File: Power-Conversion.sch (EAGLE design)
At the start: 55 parts, among them J3 AVR_SPI_PROG_3X2NS, Q1 SUM90P10-19L, U1 LM1085IS-3.3, U2 ATMEGA328P_TQFP, U7 LM2678

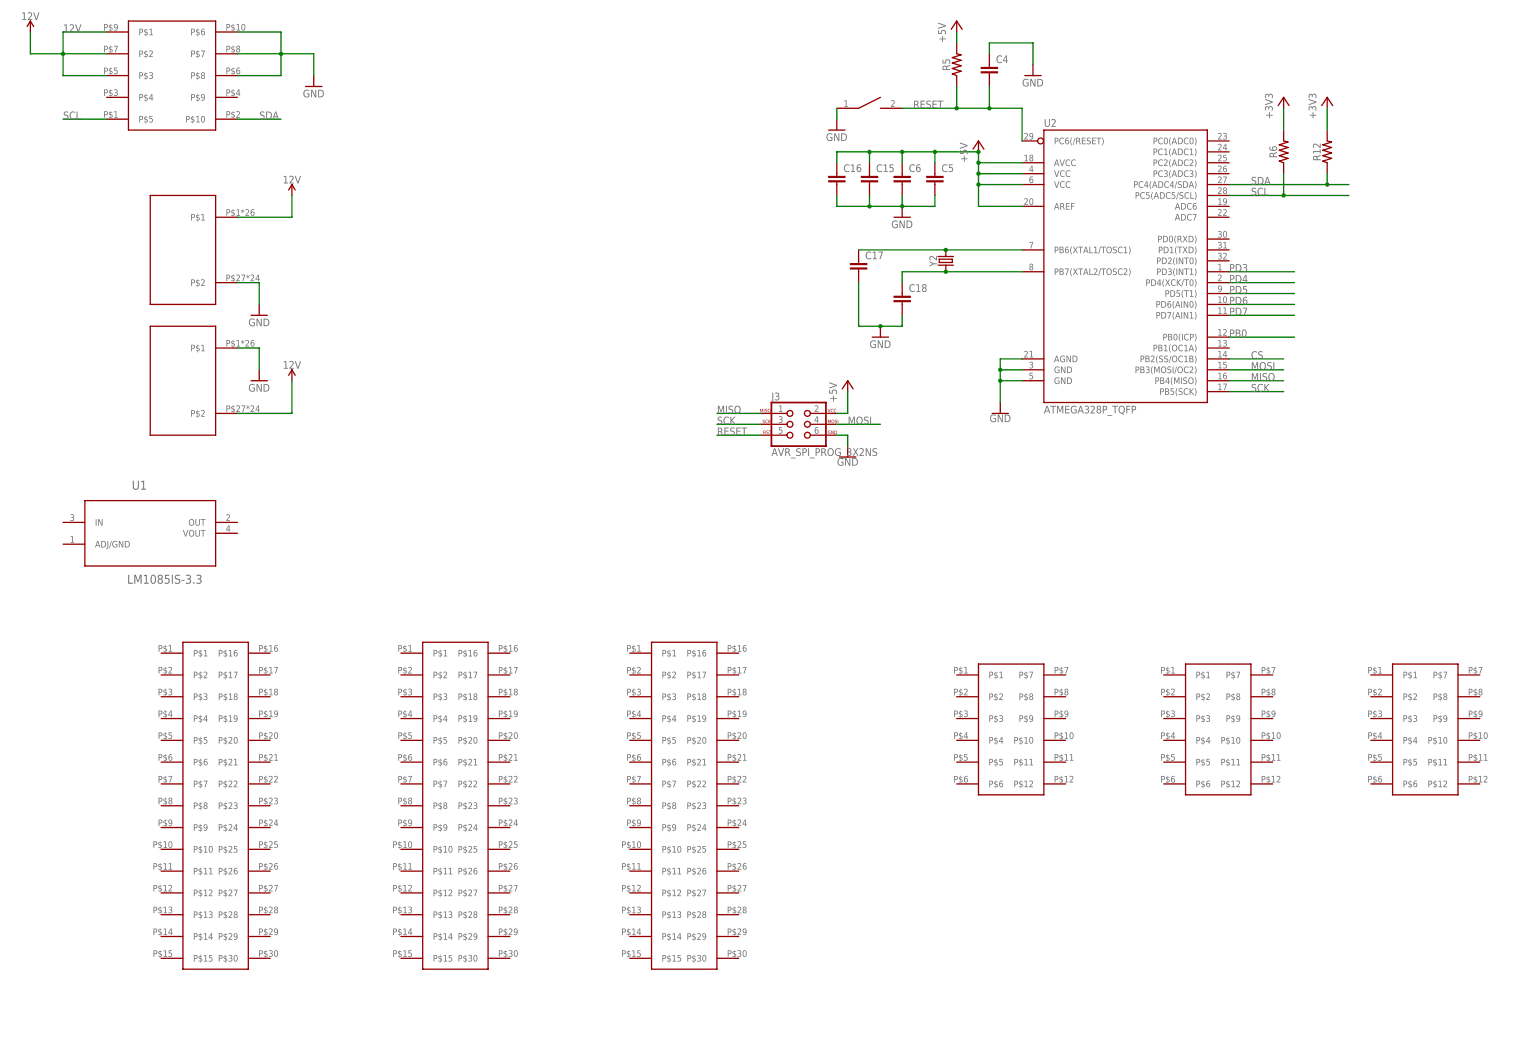
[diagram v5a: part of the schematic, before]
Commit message: Removed micro
removed micro controller and added capacitors to linear regelator
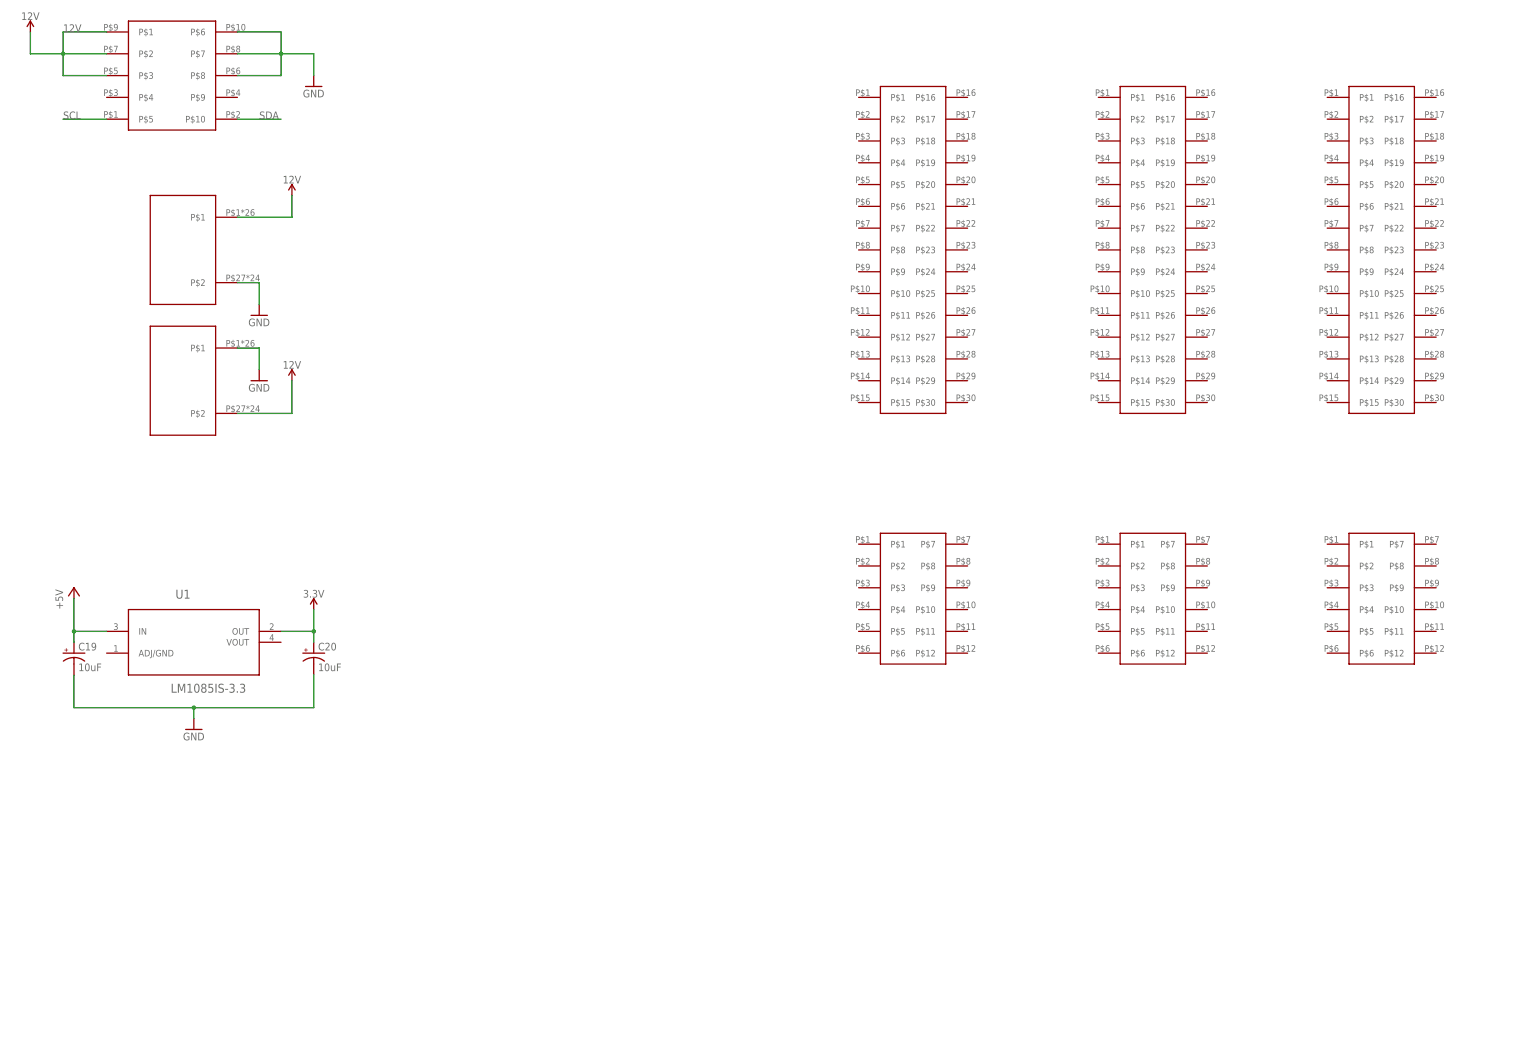
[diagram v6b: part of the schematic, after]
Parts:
- removed C15, C16, C17, C18, C4, C5, C6: (no value), rcl:C-EUC0603
- removed J3: AVR_SPI_PROG_3X2NS, SparkFun-Connectors:AVR_SPI_PROG_3X2NS
- removed R12, R5, R6: (no value), SparkFun-Resistors:RESISTOR0603
- removed RESET: SWITCH, DiscreteComponents:SWITCH
- removed U2: ATMEGA328P_TQFP, SparkFun-IC-Microcontroller:ATMEGA328P_TQFP
- removed Y2: (no value), SparkFun-Clocks:CRYSTALPTH-HC49US
- added C19, C20: 10uF, PowerComponents:C-TANTALUM(10UF_150UF)
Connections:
- removed net +3V3: R12.2, R6.2
- removed net CS: U2.PB2(SS/OC1B)
- removed net MISO: J3.1, U2.PB4(MISO)
- removed net MOSI: J3.4, U2.PB3(MOSI/OC2)
- removed net N$14: C17.1, U2.PB6(XTAL1/TOSC1), Y2.2
- removed net N$15: C18.1, U2.PB7(XTAL2/TOSC2), Y2.1
- removed net PB0: U2.PB0(ICP)
- removed net PD3: U2.PD3(INT1)
- removed net PD4: U2.PD4(XCK/T0)
- removed net PD5: U2.PD5(T1)
- removed net PD6: U2.PD6(AIN0)
- removed net PD7: U2.PD7(AIN1)
- removed net RESET: C4.2, J3.5, R5.1, RESET.P$2, U2.PC6(/RESET)
- removed net SCK: J3.3, U2.PB5(SCK)
- new net 3.3V: C20.+, U1.OUT
- net +5V: now also C19.+, U1.IN; no longer C15.1, C16.1, C5.1, C6.1, J3.2, R5.2, U2.AREF, U2.AVCC, U2.VCC@4, U2.VCC@6
- net GND: now also C19.-, C20.-; no longer C15.2, C16.2, C17.2, C18.2, C4.1, C5.2, C6.2, J3.6, RESET.P$1, U2.AGND, U2.GND@3, U2.GND@5
- net SCL: no longer R6.1, U2.PC5(ADC5/SCL)
- net SDA: no longer R12.1, U2.PC4(ADC4/SDA)
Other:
- moved on the sheet: U1

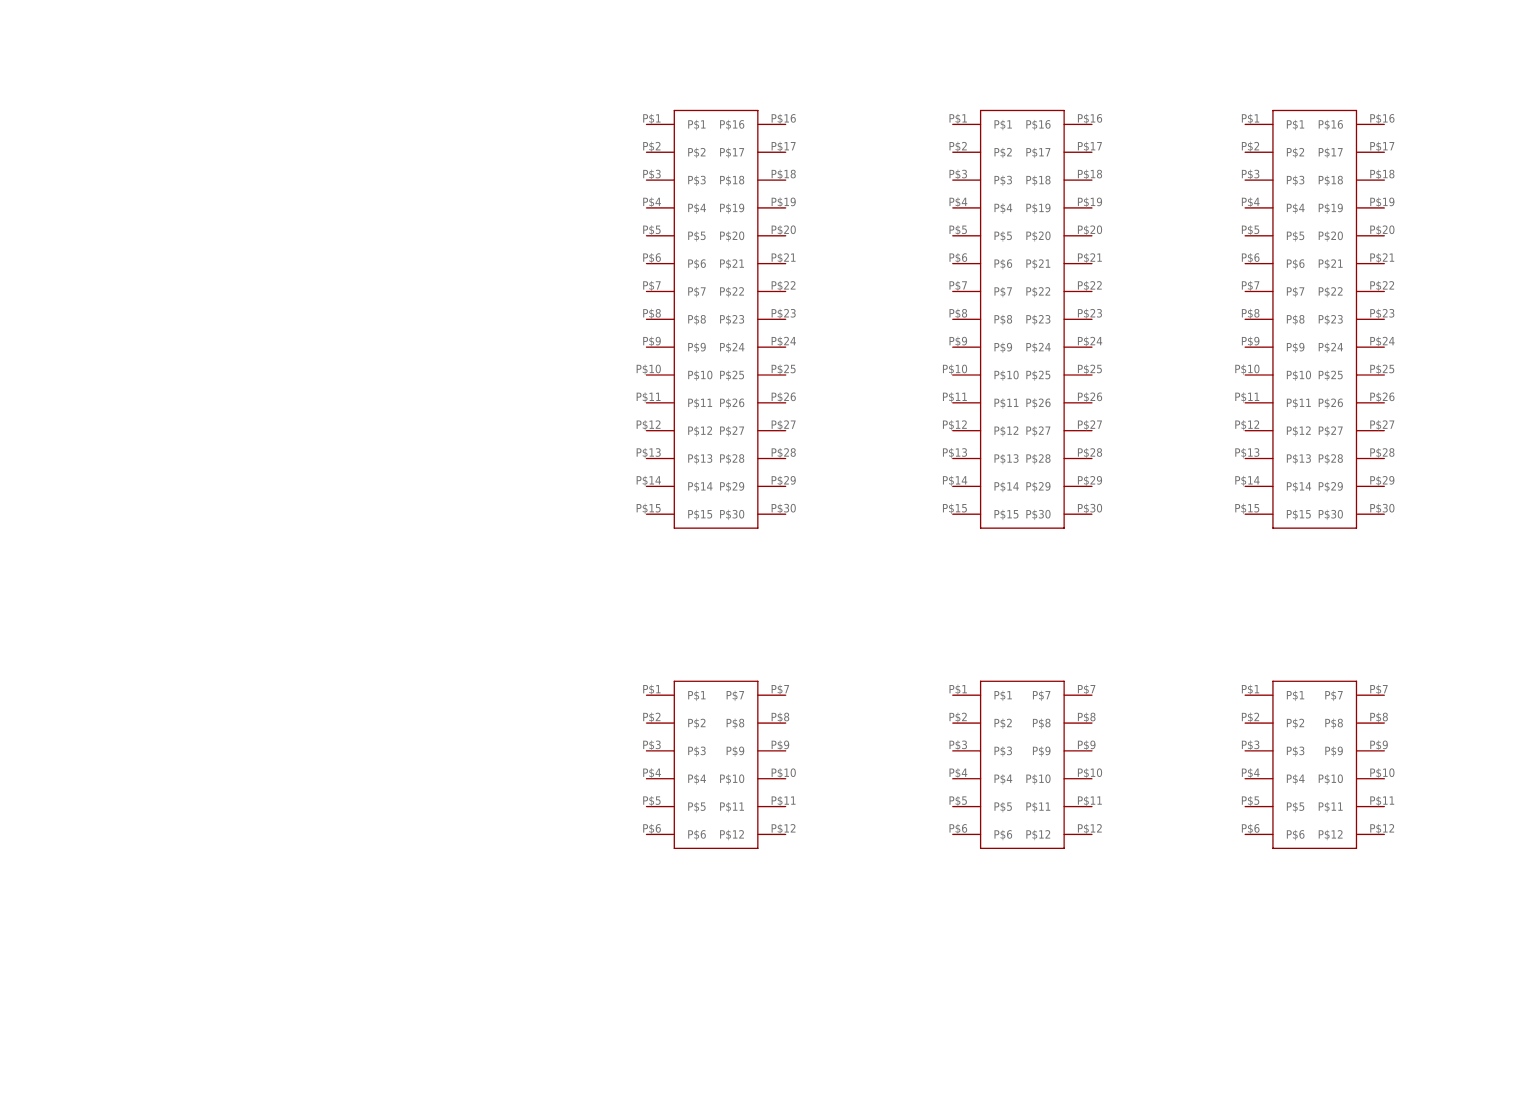
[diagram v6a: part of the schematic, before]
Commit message: Connected the connectors
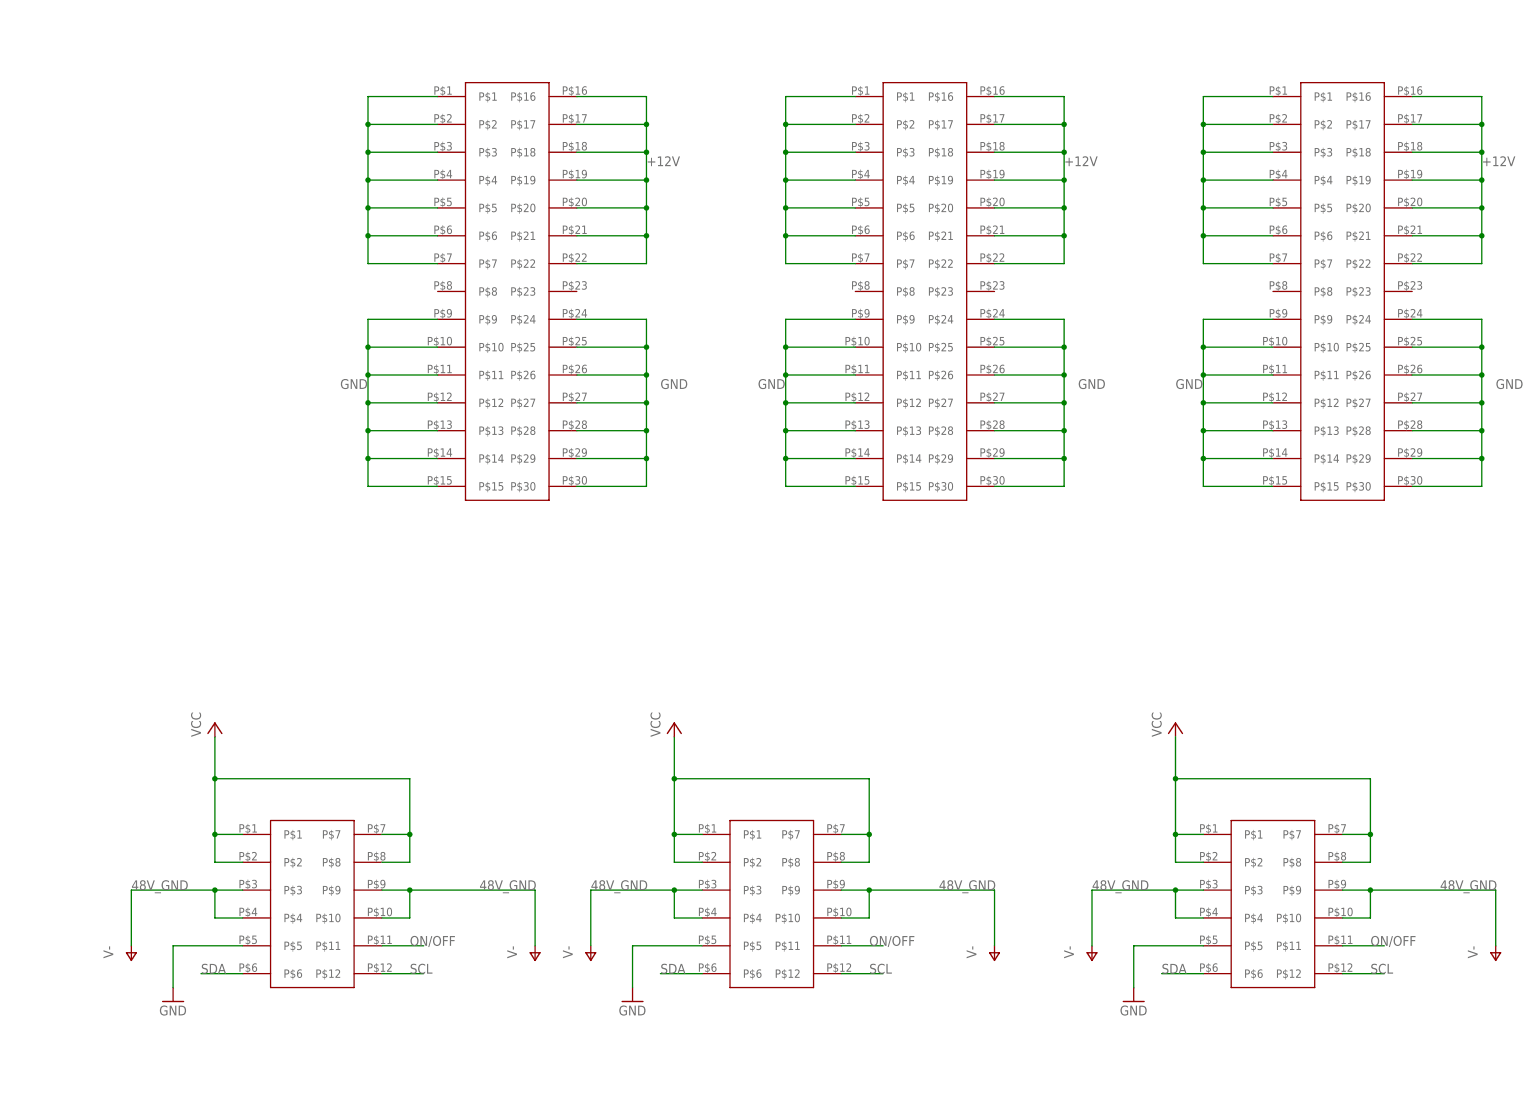
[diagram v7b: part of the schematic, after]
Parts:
- removed U$16: POWER_BRICK_CONNECTORS(2X6), MotherBoardParts2:POWER_BRICK_CONNECTORS(2X6)
- added U$17: POWER_BRICK_CONNECTORS(2X15), MotherBoardParts2:POWER_BRICK_CONNECTORS(2X15)
- U$13: value POWER_BRICK_CONNECTORS(2X15) -> POWER_BRICK_CONNECTORS(2X6); device MotherBoardParts2:POWER_BRICK_CONNECTORS(2X15) -> MotherBoardParts2:POWER_BRICK_CONNECTORS(2X6)
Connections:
- new net ON/OFF: U$13.P$11, U$14.P$11, U$15.P$11
- new net VCC: U$13.P$1, U$13.P$2, U$13.P$7, U$13.P$8, U$14.P$1, U$14.P$2, U$14.P$7, U$14.P$8, U$15.P$1, U$15.P$2, U$15.P$7, U$15.P$8
- net +12V: now also U$11.P$1, U$11.P$16, U$11.P$17, U$11.P$18, U$11.P$19, U$11.P$2, U$11.P$20, U$11.P$21, U$11.P$22, U$11.P$3, U$11.P$4, U$11.P$5, U$11.P$6, U$11.P$7, U$12.P$1, U$12.P$16, U$12.P$17, U$12.P$18, U$12.P$19, U$12.P$2, U$12.P$20, U$12.P$21, U$12.P$22, U$12.P$3, U$12.P$4, U$12.P$5, U$12.P$6, U$12.P$7, U$17.P$1, U$17.P$16, U$17.P$17, U$17.P$18, U$17.P$19, U$17.P$2, U$17.P$20, U$17.P$21, U$17.P$22, U$17.P$3, U$17.P$4, U$17.P$5, U$17.P$6, U$17.P$7
- net 48V_GND: now also U$13.P$10, U$13.P$3, U$13.P$4, U$13.P$9, U$14.P$10, U$14.P$3, U$14.P$4, U$14.P$9, U$15.P$10, U$15.P$3, U$15.P$4, U$15.P$9
- net GND: now also U$11.P$10, U$11.P$11, U$11.P$12, U$11.P$13, U$11.P$14, U$11.P$15, U$11.P$24, U$11.P$25, U$11.P$26, U$11.P$27, U$11.P$28, U$11.P$29, U$11.P$30, U$11.P$9, U$12.P$10, U$12.P$11, U$12.P$12, U$12.P$13, U$12.P$14, U$12.P$15, U$12.P$24, U$12.P$25, U$12.P$26, U$12.P$27, U$12.P$28, U$12.P$29, U$12.P$30, U$12.P$9, U$13.P$5, U$14.P$5, U$15.P$5, U$17.P$10, U$17.P$11, U$17.P$12, U$17.P$13, U$17.P$14, U$17.P$15, U$17.P$24, U$17.P$25, U$17.P$26, U$17.P$27, U$17.P$28, U$17.P$29, U$17.P$30, U$17.P$9
- net SCL: now also U$13.P$12, U$14.P$12, U$15.P$12
- net SDA: now also U$13.P$6, U$14.P$6, U$15.P$6

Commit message: Started Board layout
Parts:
- removed C19, C20: 10uF, PowerComponents:C-TANTALUM(10UF_150UF)
- removed U1: LM1085IS-3.3, PowerComponents:LM1085IS-3.3
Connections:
- removed net 3.3V: C20.+, U1.OUT
- net +5V: no longer C19.+, U1.IN
- net GND: no longer C19.-, C20.-
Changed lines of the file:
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@@
 <part name="GND5" library="supply1" deviceset="GND" device=""/>
 <part name="SUPPLY3" library="SparkFun-PowerSymbols" deviceset="12V" device=""/>
-<part name="U1" library="PowerComponents" deviceset="LM1085IS-3.3" device=""/>
-<part name="C19" library="PowerComponents" deviceset="C-TANTALUM(10UF_150UF)" device="" value="10uF"/>
-<part name="C20" library="PowerComponents" deviceset="C-TANTALUM(10UF_150UF)" device="" value="10uF"/>
-<part name="GND6" library="supply1" deviceset="GND" device=""/>
-<part name="P+6" library="supply1" library_urn="urn:adsk.eagle:library:371" deviceset="+5V" device=""/>
-<part name="SUPPLY4" library="SparkFun-PowerSymbols" deviceset="3.3V" device=""/>
 <part name="U$17" library="MotherBoardParts2" deviceset="POWER_BRICK_CONNECTORS(2X15)" device=""/>
 <part name="U$11" library="MotherBoardParts2" deviceset="POWER_BRICK_CONNECTORS(2X15)" device=""/>
@@
 <instance part="GND5" gate="1" x="83.82" y="502.92"/>
 <instance part="SUPPLY3" gate="G$1" x="17.78" y="515.62"/>
-<instance part="U1" gate="A" x="55.88" y="375.92"/>
-<instance part="C19" gate="G$1" x="27.94" y="370.84"/>
-<instance part="C20" gate="G$1" x="83.82" y="370.84"/>
-<instance part="GND6" gate="1" x="55.88" y="353.06"/>
-<instance part="P+6" gate="1" x="27.94" y="386.08"/>
-<instance part="SUPPLY4" gate="G$1" x="83.82" y="381"/>
 <instance part="U$17" gate="G$1" x="185.42" y="472.44"/>
 <instance part="U$11" gate="G$1" x="261.62" y="472.44"/>
@@
 </segment>
 <segment>
-<pinref part="C19" gate="G$1" pin="-"/>
-<wire x1="27.94" y1="365.76" x2="27.94" y2="358.14" width="0.1524" layer="91"/>
-<pinref part="C20" gate="G$1" pin="-"/>
-<wire x1="27.94" y1="358.14" x2="55.88" y2="358.14" width="0.1524" layer="91"/>
-<wire x1="55.88" y1="358.14" x2="83.82" y2="358.14" width="0.1524" layer="91"/>
-<wire x1="83.82" y1="358.14" x2="83.82" y2="365.76" width="0.1524" layer="91"/>
-<pinref part="GND6" gate="1" pin="GND"/>
-<wire x1="55.88" y1="355.6" x2="55.88" y2="358.14" width="0.1524" layer="91"/>
-<junction x="55.88" y="358.14"/>
-</segment>
-<segment>
 <pinref part="U$17" gate="G$1" pin="P$15"/>
 <wire x1="172.72" y1="434.34" x2="160.02" y2="434.34" width="0.1524" layer="91"/>
@@
 <junction x="172.72" y="114.3"/>
 </segment>
-<segment>
-<pinref part="C19" gate="G$1" pin="+"/>
-<wire x1="27.94" y1="373.38" x2="27.94" y2="375.92" width="0.1524" layer="91"/>
-<pinref part="U1" gate="A" pin="IN"/>
-<wire x1="27.94" y1="375.92" x2="35.56" y2="375.92" width="0.1524" layer="91"/>
-<pinref part="P+6" gate="1" pin="+5V"/>
-<wire x1="27.94" y1="375.92" x2="27.94" y2="383.54" width="0.1524" layer="91"/>
-<junction x="27.94" y="375.92"/>
-</segment>
 </net>
 <net name="N$25" class="0">
@@
 </segment>
 </net>
-<net name="3.3V" class="0">
-<segment>
-<pinref part="U1" gate="A" pin="OUT"/>
-<pinref part="C20" gate="G$1" pin="+"/>
-<wire x1="76.2" y1="375.92" x2="83.82" y2="375.92" width="0.1524" layer="91"/>
-<wire x1="83.82" y1="375.92" x2="83.82" y2="373.38" width="0.1524" layer="91"/>
-<pinref part="SUPPLY4" gate="G$1" pin="3.3V"/>
-<wire x1="83.82" y1="375.92" x2="83.82" y2="381" width="0.1524" layer="91"/>
-<junction x="83.82" y="375.92"/>
-</segment>
-</net>
